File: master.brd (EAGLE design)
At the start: 69.5 x 66 mm, 31 parts, among them IC1 ATMEGA328-P, U2 ENC28J60-SO, Y2 25MHz, Y3 16MHz

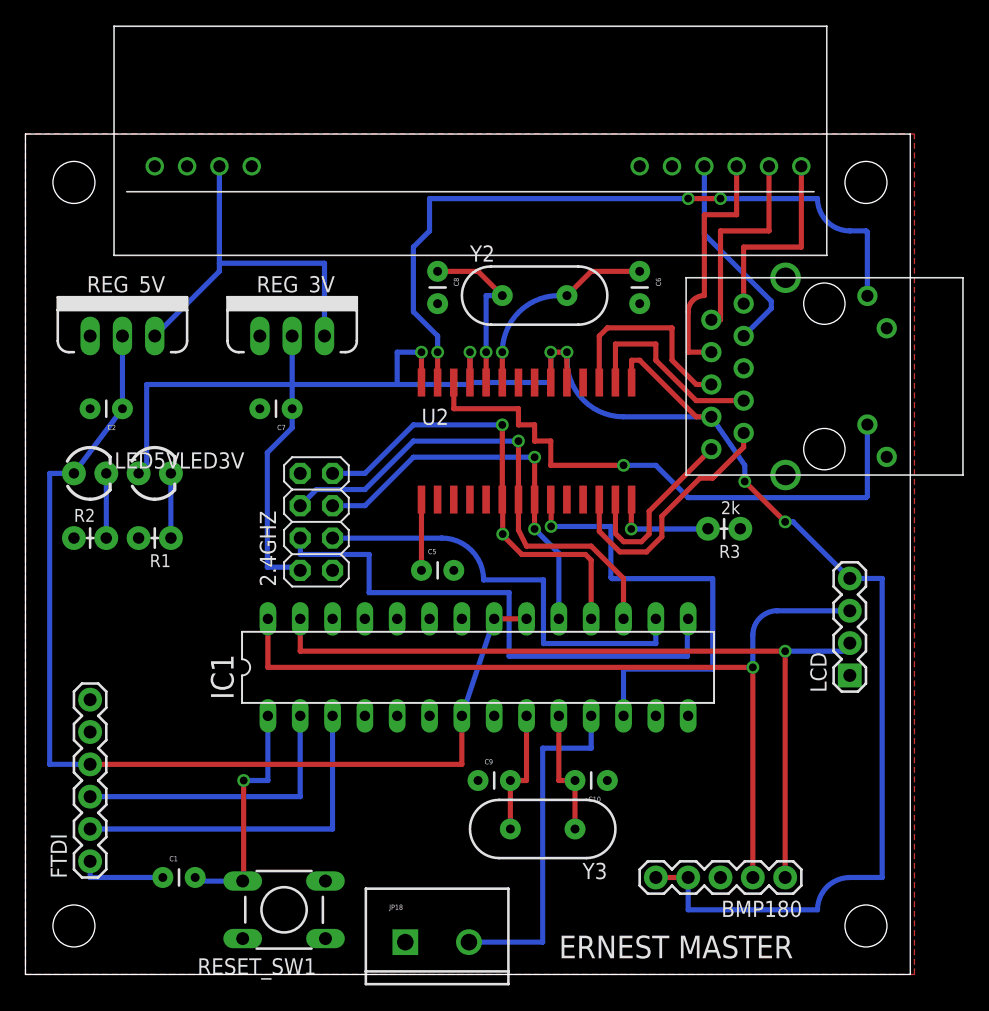
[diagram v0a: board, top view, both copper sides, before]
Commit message: Use SMD Atmega
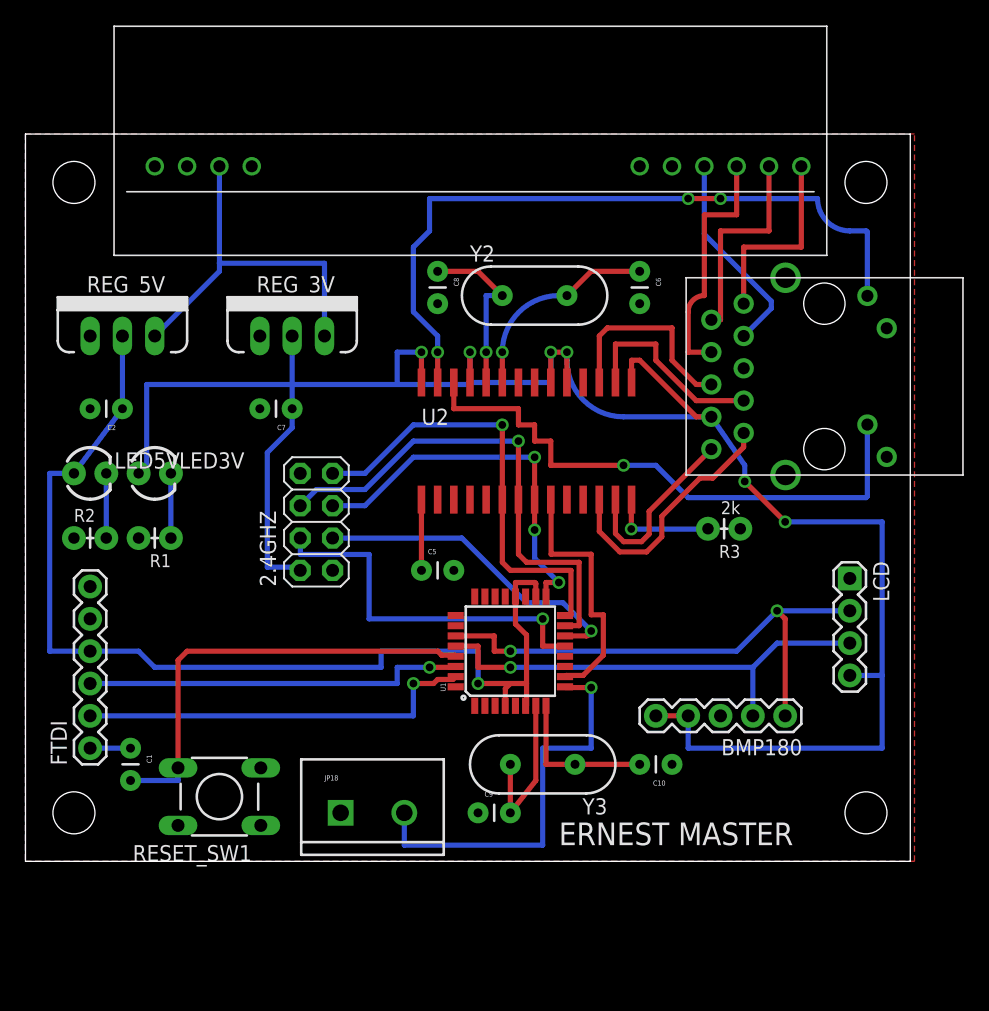
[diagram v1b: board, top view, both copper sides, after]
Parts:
- removed IC1: ATMEGA328-P, Arduino-AVR:DIL28-3
- added U1: ATMEGA328P_TQFP, SparkFun-DigitalIC:TQFP32-08
- moved BMP180 12.7 mm to (59.7, 20.3)
- moved JP18 11.4 mm to (24.8, 12.7)
- moved C1 10.5 mm to (8.26, 17.8), turned to 270 degrees
- moved RESET_SW1 10.2 mm to (15.2, 14.0)
- moved FTDI 8.89 mm to (5.08, 17.8)
- moved STANDOFF2 8.89 mm to (3.81, 12.7)
- moved STANDOFF3 8.89 mm to (66.0, 12.7)
- moved LCD 7.62 mm to (64.8, 31.1), turned to 270 degrees
- moved C10 5.24 mm to (50.8, 16.5)
- moved Y3 5.08 mm to (40.6, 16.5)
- moved C9 2.54 mm to (35.6, 12.7)
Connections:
- net 5V: now also U1.18, U1.20, U1.4, U1.6; no longer IC1.20, IC1.21, IC1.7
- net E_CS: now also U1.10; no longer IC1.12
- net FTDI_RX: now also U1.31; no longer IC1.3
- net FTDI_TX: now also U1.30; no longer IC1.2
- net GND: now also U1.21, U1.3, U1.5; no longer IC1.22, IC1.8
- net MISO: now also U1.16; no longer IC1.18
- net MOSI: now also U1.15; no longer IC1.17
- net N$20: now also U1.7; no longer IC1.9
- net N$21: now also U1.8; no longer IC1.10
- net RELAY: now also U1.9; no longer IC1.11
- net RESET: now also U1.29; no longer IC1.1
- net R_CE: now also U1.14; no longer IC1.16
- net R_CSN: now also U1.13; no longer IC1.15
- net SCK: now also U1.17; no longer IC1.19
- net SCL: now also U1.28; no longer IC1.28
- net SDA: now also U1.27; no longer IC1.27
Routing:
- net SCL: track 69.4 -> 37.2 mm
- net SDA: track 63.8 -> 42.0 mm, vias 1 -> 2
- net E_CS: track 36.7 -> 20.0 mm, vias 1 -> 0
- net RESET: track 19.0 -> 35.5 mm, vias 1 -> 0
- net R_CSN: track 42.7 -> 29.3 mm, vias 0 -> 1
- net R_CE: track 33.7 -> 25.6 mm, vias 0 -> 1
- net FTDI_TX: track 22.9 -> 30.1 mm, vias 0 -> 1
- net 3.3V: track 169.6 -> 163.5 mm
- net RELAY: track 27.4 -> 31.7 mm, vias 0 -> 1
- net N$37: track 6.99 -> 3.18 mm
- net FTDI_RX: track 27.9 -> 31.5 mm, vias 0 -> 1
- net N$20: track 10.2 -> 12.9 mm
- net N$21: track 10.2 -> 12.0 mm
- net 5V: track 83.6 -> 84.4 mm, vias 0 -> 1
- net SCK: track 30.9 -> 30.2 mm, vias 2 -> 3
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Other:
- board size 69.5 x 66 mm -> 69.5 x 57.1 mm

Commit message: Fix LM7805 pinout
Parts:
- added C3: 0.1uF, SparkFun-Capacitors:CAP-PTH-SMALL
- added U$1: HIH6131, SparkFun-AnalogIC:SOIC8
- REG_5V: value LM1117 -> LM7805
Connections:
- new net N$17: C3.1, U$1.1
- net 3.3V: now also U$1.8
- net 5V: now also REG_5V.3; no longer REG_5V.2
- net GND: now also C3.2, REG_5V.2, U$1.2; no longer REG_5V.1
- net POE_IN: now also REG_5V.1; no longer REG_5V.3
- net SCL: now also U$1.3
- net SDA: now also U$1.4
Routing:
- net SCL: track 37.2 -> 56.9 mm
- net SDA: track 42.0 -> 61.5 mm
- net 3.3V: track 163.5 -> 183.0 mm, vias 6 -> 7
- net POE_IN: track 29.4 -> 37.5 mm
- net N$17: track 0.00 -> 4.69 mm
- net 5V: track 84.4 -> 86.9 mm
- net N$20: track 12.9 -> 10.4 mm
- net RESET: track 35.5 -> 35.4 mm, vias 0 -> 1
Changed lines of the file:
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@@
 <layer number="31" name="tCream" color="7" fill="4" visible="no" active="yes"/>
 <layer number="32" name="bCream" color="7" fill="5" visible="no" active="yes"/>
-<layer number="33" name="tFinish" color="6" fill="3" visible="no" active="yes"/>
-<layer number="34" name="bFinish" color="6" fill="6" visible="no" active="yes"/>
-<layer number="35" name="tGlue" color="7" fill="4" visible="no" active="yes"/>
-<layer number="36" name="bGlue" color="7" fill="5" visible="no" active="yes"/>
-<layer number="37" name="tTest" color="7" fill="1" visible="no" active="yes"/>
-<layer number="38" name="bTest" color="7" fill="1" visible="no" active="yes"/>
+<layer number="33" name="tFinish" color="6" fill="3" visible="yes" active="yes"/>
+<layer number="34" name="bFinish" color="6" fill="6" visible="yes" active="yes"/>
+<layer number="35" name="tGlue" color="7" fill="4" visible="yes" active="yes"/>
+<layer number="36" name="bGlue" color="7" fill="5" visible="yes" active="yes"/>
+<layer number="37" name="tTest" color="7" fill="1" visible="yes" active="yes"/>
+<layer number="38" name="bTest" color="7" fill="1" visible="yes" active="yes"/>
 <layer number="39" name="tKeepout" color="4" fill="11" visible="yes" active="yes"/>
 <layer number="40" name="bKeepout" color="1" fill="11" visible="yes" active="yes"/>
@@
 <layer number="43" name="vRestrict" color="2" fill="10" visible="yes" active="yes"/>
 <layer number="44" name="Drills" color="7" fill="1" visible="no" active="yes"/>
-<layer number="45" name="Holes" color="7" fill="1" visible="yes" active="yes"/>
-<layer number="46" name="Milling" color="3" fill="1" visible="no" active="yes"/>
-<layer number="47" name="Measures" color="7" fill="1" visible="no" active="yes"/>
+<layer number="45" name="Holes" color="7" fill="1" visible="no" active="yes"/>
+<layer number="46" name="Milling" color="3" fill="1" visible="yes" active="yes"/>
+<layer number="47" name="Measures" color="7" fill="1" visible="yes" active="yes"/>
 <layer number="48" name="Document" color="7" fill="1" visible="yes" active="yes"/>
 <layer number="49" name="Reference" color="7" fill="1" visible="yes" active="yes"/>
@@
 <wire x1="69.52" y1="66.03" x2="0" y2="66.03" width="0" layer="20"/>
 <wire x1="0" y1="66.03" x2="0" y2="8.89" width="0" layer="20"/>
-<text x="41.91" y="10.16" size="1.778" layer="112">ERNEST MASTER</text>
+<text x="41.91" y="10.16" size="1.778" layer="121">ERNEST MASTER</text>
 </plain>
 <attributes>
@@
 <element name="C9" library="SparkFun-Capacitors" package="CAP-PTH-SMALL" value="22pF" x="35.56" y="12.7"/>
 <element name="C10" library="SparkFun-Capacitors" package="CAP-PTH-SMALL" value="22pF" x="50.8" y="16.51" rot="R180"/>
-<element name="REG_5V" library="User-Submitted" package="TO220V" value="LM1117" x="7.62" y="50.165"/>
 <element name="2.4GHZ" library="adafruit" package="2X04" value="" x="22.86" y="35.56" rot="R90"/>
 <element name="U$2" library="SmartPrj" package="AG9000" value="AG9XX0" x="60.96" y="63.5" rot="R180"/>
@@
 <attribute name="PROD_ID" value="IC-09069" x="38.1" y="25.4" size="1.778" layer="27" rot="R90" display="off"/>
 </element>
+<element name="U$1" library="SparkFun-AnalogIC" package="SOIC8" value="HIH6131" x="13.97" y="26.9875" rot="R90"/>
+<element name="C3" library="SparkFun-Capacitors" package="CAP-PTH-SMALL" value="0.1uF" x="20.6375" y="25.7175"/>
+<element name="REG_5V" library="User-Submitted" package="TO220V" value="LM7805" x="7.62" y="50.165"/>
 </elements>
 <signals>
@@
 <contactref element="C6" pad="2"/>
 <contactref element="C8" pad="2"/>
-<contactref element="REG_5V" pad="1"/>
 <contactref element="2.4GHZ" pad="1"/>
 <contactref element="U$2" pad="P$7"/>
@@
 <contactref element="U1" pad="3"/>
 <contactref element="U1" pad="5"/>
+<contactref element="U$1" pad="2"/>
+<contactref element="C3" pad="2"/>
+<contactref element="REG_5V" pad="2"/>
 </signal>
 <signal name="E_CS">
@@
 <wire x1="59.055" y1="26.035" x2="64.77" y2="26.035" width="0.4064" layer="16"/>
 <wire x1="57.15" y1="24.13" x2="57.15" y2="20.32" width="0.4064" layer="16"/>
+<contactref element="U$1" pad="3"/>
+<wire x1="33.8074" y1="25.8" x2="26.67" y2="25.8" width="0.4064" layer="1"/>
+<wire x1="26.67" y1="25.8" x2="26.67" y2="27.94" width="0.4064" layer="1"/>
+<wire x1="26.67" y1="27.94" x2="18.415" y2="27.94" width="0.4064" layer="1"/>
+<wire x1="18.415" y1="27.94" x2="18.415" y2="27.6225" width="0.4064" layer="1"/>
+<wire x1="18.415" y1="27.6225" x2="16.5862" y2="27.6225" width="0.4064" layer="1"/>
 </signal>
 <signal name="SDA">
@@
 <wire x1="59.69" y1="20.32" x2="59.69" y2="27.94" width="0.4064" layer="1"/>
 <wire x1="59.69" y1="27.94" x2="59.055" y2="28.575" width="0.4064" layer="1"/>
+<contactref element="U$1" pad="4"/>
+<wire x1="33.8074" y1="26.6" x2="27.94" y2="26.6" width="0.4064" layer="1"/>
+<wire x1="27.94" y1="26.6" x2="27.94" y2="28.8925" width="0.4064" layer="1"/>
+<wire x1="27.94" y1="28.8925" x2="16.5862" y2="28.8925" width="0.4064" layer="1"/>
 </signal>
 <signal name="MOSI">
@@
 <wire x1="30.48" y1="20.32" x2="30.48" y2="22.86" width="0.4064" layer="16"/>
 <via x="30.48" y="22.86" extent="1-16" drill="0.6096"/>
-<wire x1="30.48" y1="22.86" x2="32.0675" y2="22.86" width="0.4064" layer="1"/>
-<wire x1="32.0675" y1="22.86" x2="32.385" y2="23.1775" width="0.4064" layer="1"/>
-<wire x1="32.385" y1="23.1775" x2="33.5849" y2="23.1775" width="0.4064" layer="1"/>
-<wire x1="33.5849" y1="23.1775" x2="33.8074" y2="23.4" width="0.4064" layer="1"/>
+<wire x1="33.8074" y1="23.4" x2="32.385" y2="23.4" width="0.4064" layer="1"/>
+<wire x1="32.385" y1="23.4" x2="32.385" y2="22.86" width="0.4064" layer="1"/>
+<wire x1="32.385" y1="22.86" x2="30.48" y2="22.86" width="0.4064" layer="1"/>
 </signal>
 <signal name="3.3V">
@@
 <wire x1="52.07" y1="17.78" x2="67.31" y2="17.78" width="0.4064" layer="16"/>
 <wire x1="67.31" y1="17.78" x2="67.31" y2="23.495" width="0.4064" layer="16"/>
+<contactref element="U$1" pad="8"/>
+<wire x1="11.3538" y1="25.0825" x2="8.89" y2="25.0825" width="0.4064" layer="1"/>
+<wire x1="8.89" y1="25.0825" x2="8.89" y2="26.67" width="0.4064" layer="1"/>
+<via x="8.89" y="26.67" extent="1-16" drill="0.6096"/>
+<wire x1="19" y1="32" x2="8.89" y2="32" width="0.4064" layer="16"/>
+<wire x1="8.89" y1="32" x2="8.89" y2="26.67" width="0.4064" layer="16"/>
 </signal>
 <signal name="5V">
@@
 <contactref element="FTDI" pad="4"/>
 <contactref element="LED5V" pad="A"/>
-<contactref element="REG_5V" pad="2"/>
-<wire x1="7.62" y1="50.165" x2="7.62" y2="44.45" width="0.4064" layer="16"/>
 <wire x1="7.62" y1="44.45" x2="3.81" y2="39.37" width="0.4064" layer="16"/>
 <wire x1="3.81" y1="39.37" x2="1.905" y2="39.37" width="0.4064" layer="16"/>
@@
 <via x="35.56" y="22.86" extent="1-16" drill="0.6096"/>
 <wire x1="35.56" y1="22.86" x2="38.1" y2="22.86" width="0.4064" layer="1"/>
+<contactref element="REG_5V" pad="3"/>
+<wire x1="10.16" y1="50.165" x2="10.16" y2="47.3075" width="0.4064" layer="16"/>
+<wire x1="10.16" y1="47.3075" x2="7.62" y2="47.3075" width="0.4064" layer="16"/>
+<wire x1="7.62" y1="47.3075" x2="7.62" y2="44.45" width="0.4064" layer="16"/>
 </signal>
 <signal name="N$37">
@@
 <contactref element="Y3" pad="2"/>
 <contactref element="C9" pad="2"/>
-<wire x1="40.1" y1="15.24" x2="38.1" y2="12.7" width="0.4064" layer="1"/>
-<wire x1="38.1" y1="12.7" x2="38.1" y2="16.51" width="0.4064" layer="1"/>
 <contactref element="U1" pad="7"/>
-<wire x1="40.1" y1="21.1074" x2="40.1" y2="15.24" width="0.4064" layer="1"/>
+<wire x1="40.1" y1="21.1074" x2="40.1" y2="16.51" width="0.4064" layer="1"/>
+<wire x1="40.1" y1="16.51" x2="38.1" y2="16.51" width="0.4064" layer="1"/>
+<wire x1="38.1" y1="16.51" x2="38.1" y2="12.7" width="0.4064" layer="1"/>
 </signal>
 <signal name="N$21">
@@
 <wire x1="8.255" y1="15.24" x2="11.9888" y2="15.24" width="0.4064" layer="16"/>
 <wire x1="11.9888" y1="15.24" x2="11.9888" y2="16.2306" width="0.4064" layer="16"/>
-<wire x1="11.9888" y1="16.2306" x2="11.9888" y2="24.6888" width="0.4064" layer="1"/>
-<wire x1="11.9888" y1="24.6888" x2="12.7" y2="25.4" width="0.4064" layer="1"/>
-<wire x1="12.7" y1="25.4" x2="32.385" y2="25.4" width="0.4064" layer="1"/>
-<wire x1="32.385" y1="25.4" x2="32.7025" y2="25.0825" width="0.4064" layer="1"/>
-<wire x1="32.7025" y1="25.0825" x2="33.7249" y2="25.0825" width="0.4064" layer="1"/>
 <wire x1="33.7249" y1="25.0825" x2="33.8074" y2="25" width="0.4064" layer="1"/>
+<wire x1="33.7249" y1="25.0825" x2="26.67" y2="25.0825" width="0.4064" layer="1"/>
+<wire x1="26.67" y1="25.0825" x2="26.67" y2="19.05" width="0.4064" layer="1"/>
+<via x="26.67" y="19.05" extent="1-16" drill="0.6096"/>
+<wire x1="26.67" y1="19.05" x2="11.9888" y2="19.05" width="0.4064" layer="16"/>
+<wire x1="11.9888" y1="19.05" x2="11.9888" y2="16.2306" width="0.4064" layer="16"/>
 </signal>
 <signal name="POE_IN">
 <contactref element="REG_3V" pad="3"/>
-<contactref element="REG_5V" pad="3"/>
 <contactref element="U$2" pad="P$8"/>
 <wire x1="15.24" y1="63.5" x2="15.24" y2="55.88" width="0.4064" layer="16"/>
 <wire x1="15.24" y1="55.88" x2="15.24" y2="55.245" width="0.4064" layer="16"/>
-<wire x1="15.24" y1="55.245" x2="10.16" y2="50.165" width="0.4064" layer="16"/>
 <wire x1="23.495" y1="50.165" x2="23.495" y2="55.88" width="0.4064" layer="16"/>
 <wire x1="23.495" y1="55.88" x2="15.24" y2="55.88" width="0.4064" layer="16"/>
+<contactref element="REG_5V" pad="1"/>
+<wire x1="15.24" y1="55.245" x2="5.08" y2="55.245" width="0.4064" layer="16"/>
+<wire x1="5.08" y1="55.245" x2="5.08" y2="50.165" width="0.4064" layer="16"/>
 </signal>
 <signal name="V2+">
@@
 <wire x1="56.43" y1="57.15" x2="56.43" y2="52.705" width="0.4064" layer="1"/>
 </signal>
+<signal name="N$17">
+<contactref element="C3" pad="1"/>
+<contactref element="U$1" pad="1"/>
+<wire x1="16.5862" y1="25.0825" x2="20.6375" y2="25.0825" width="0.4064" layer="1"/>
+<wire x1="20.6375" y1="25.0825" x2="20.6375" y2="25.7175" width="0.4064" layer="1"/>
+</signal>
 </signals>
